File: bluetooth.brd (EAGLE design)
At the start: 28.3 x 23.1 mm, 28 parts, among them U1 NRF8001, X1 16MHz, X2 32.768kHz

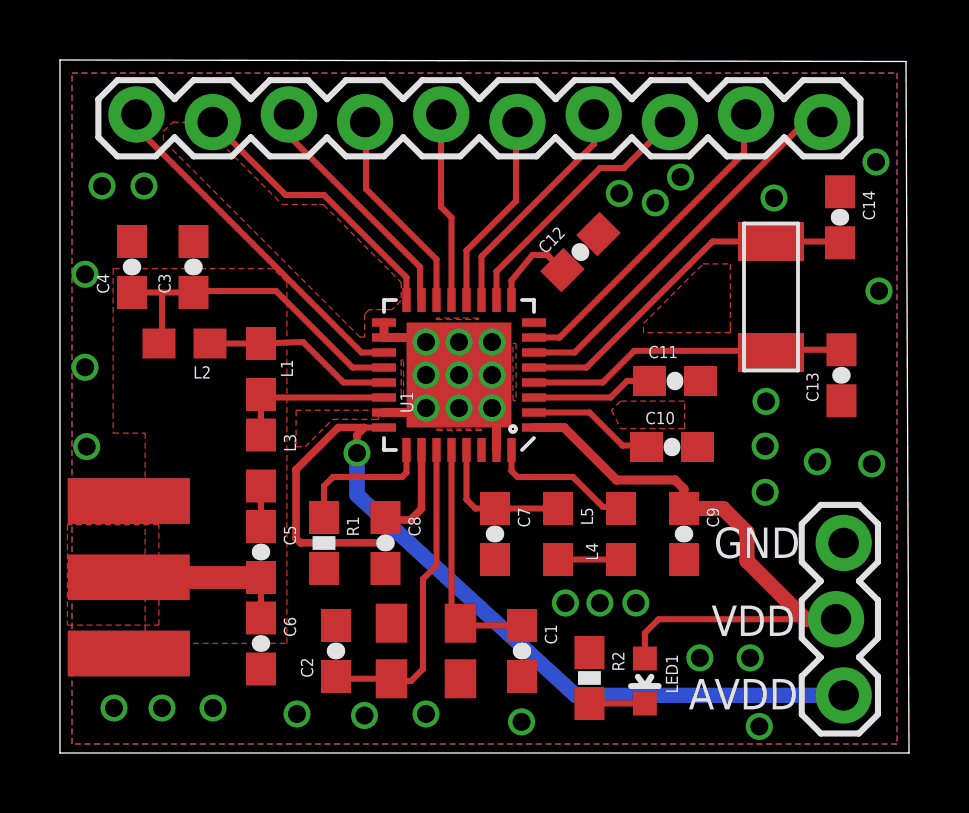
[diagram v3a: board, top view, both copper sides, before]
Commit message: Connected pin 9 (power) to VDD. Oops
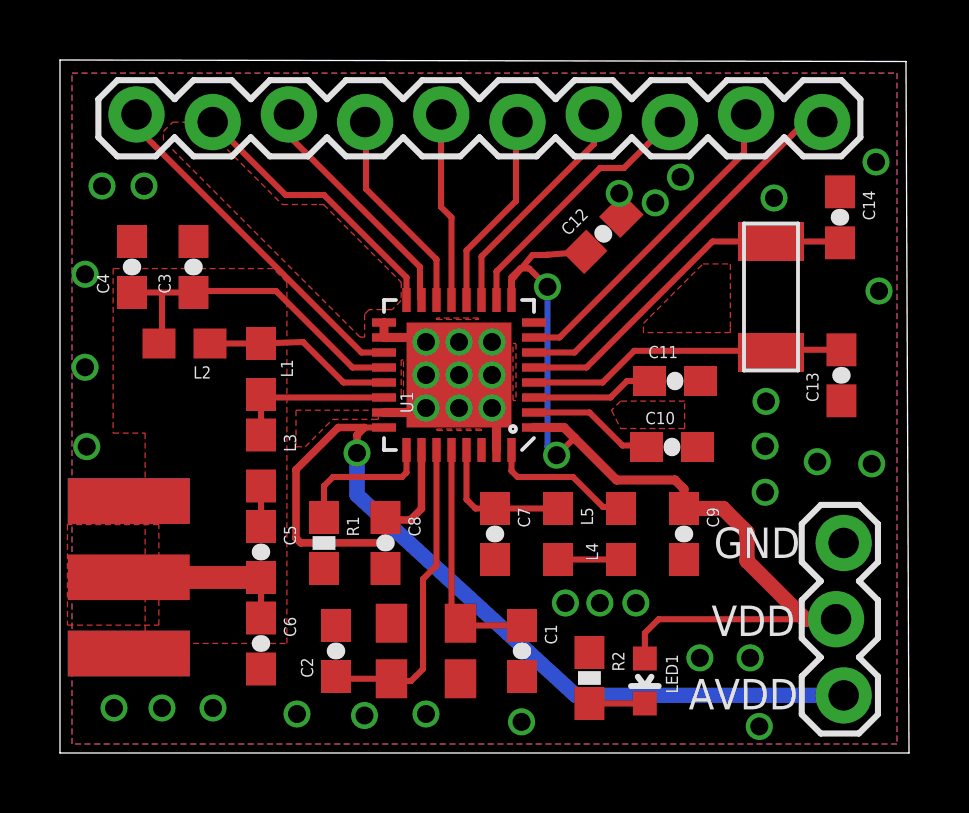
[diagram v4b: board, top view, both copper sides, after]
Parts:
- moved C12 0.98 mm to (17.7, 17.0)
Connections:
- removed net N$8: C12.1, U1.9
- net VDD: now also C12.1, U1.9
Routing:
- net VDD: track 20.5 -> 32.9 mm, vias 0 -> 2
- net N$8: track 2.99 -> 0.00 mm
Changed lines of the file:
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@@
 <setting verticaltext="up"/>
 </settings>
-<grid distance="6" unitdist="mil" unit="inch" style="lines" multiple="1" display="yes" altdistance="0.05" altunitdist="mm" altunit="mm"/>
+<grid distance="1" unitdist="mil" unit="mil" style="lines" multiple="1" display="yes" altdistance="0.05" altunitdist="mm" altunit="mm"/>
 <layers>
 <layer number="1" name="Top" color="4" fill="1" visible="yes" active="yes"/>
@@
 <element name="C13" library="SparkFun" package="0603-CAP" value="12.5pF" x="25.6476125" y="12.29040625" rot="R90"/>
 <element name="C14" library="SparkFun" package="0603-CAP" value="12.5pF" x="25.6000125" y="17.557209375" rot="R270"/>
-<element name="C12" library="SparkFun" package="0603-CAP" value="100nF" x="16.9476" y="16.3976" rot="R45"/>
+<element name="C12" library="SparkFun" package="0603-CAP" value="100nF" x="17.7096" y="17.0072" rot="R45"/>
 <element name="C3" library="SparkFun" package="0603-CAP" value="2.2nF" x="4.05" y="15.9" rot="R90"/>
 <element name="C4" library="SparkFun" package="0603-CAP" value="0" x="2" y="15.9" rot="R90"/>
@@
 <wire x1="19.250003125" y1="12.1" x2="19.250009375" y2="12.10000625" width="0.2032" layer="1"/>
 </signal>
-<signal name="N$8">
-<contactref element="U1" pad="9"/>
-<contactref element="C12" pad="1"/>
-<wire x1="14.65000625" y1="14.80000625" x2="14.65000625" y2="15.45000625" width="0.2032" layer="1"/>
-<wire x1="14.65000625" y1="15.45000625" x2="15.347609375" y2="16.300009375" width="0.2032" layer="1"/>
-<wire x1="15.347609375" y1="16.300009375" x2="15.6972" y2="16.300009375" width="0.2032" layer="1"/>
-<wire x1="15.6972" y1="16.300009375" x2="15.8496" y2="16.3068" width="0.2032" layer="1"/>
-<wire x1="15.8496" y1="16.3068" x2="15.8363125" y2="16.3068" width="0.2032" layer="1"/>
-<wire x1="15.8363125" y1="16.3068" x2="16.34655625" y2="15.79655625" width="0.2032" layer="1"/>
-</signal>
 <signal name="N$3">
 <contactref element="L3" pad="1"/>
@@
 <wire x1="20.400009375" y1="8.50000625" x2="20.100009375" y2="8.80000625" width="0.3048" layer="1"/>
 <wire x1="20.100009375" y1="8.80000625" x2="18.14999375" y2="8.80000625" width="0.3048" layer="1"/>
-<wire x1="18.14999375" y1="8.80000625" x2="16.4" y2="10.55" width="0.3048" layer="1"/>
+<wire x1="18.14999375" y1="8.80000625" x2="16.7516" y2="10.1984" width="0.3048" layer="1"/>
+<wire x1="16.7516" y1="10.1984" x2="16.4" y2="10.55" width="0.3048" layer="1"/>
 <wire x1="16.4" y1="10.55" x2="15.4000125" y2="10.55" width="0.3048" layer="1"/>
 <wire x1="15.4000125" y1="10.55" x2="15.40000625" y2="10.55000625" width="0.3048" layer="1"/>
@@
 <vertex x="12.15" y="10.45"/>
 </polygon>
+<contactref element="U1" pad="9"/>
+<contactref element="C12" pad="1"/>
+<wire x1="14.65000625" y1="14.80000625" x2="14.65000625" y2="15.45000625" width="0.2032" layer="1"/>
+<wire x1="14.65000625" y1="15.45000625" x2="15.347609375" y2="16.300009375" width="0.2032" layer="1"/>
+<wire x1="15.347609375" y1="16.300009375" x2="15.6972" y2="16.300009375" width="0.2032" layer="1"/>
+<wire x1="15.6972" y1="16.300009375" x2="15.8496" y2="16.3068" width="0.2032" layer="1"/>
+<wire x1="15.8496" y1="16.3068" x2="15.8363125" y2="16.3068" width="0.2032" layer="1"/>
+<wire x1="15.8363125" y1="16.3068" x2="17.10855625" y2="16.40615625" width="0.2032" layer="1"/>
+<wire x1="14.65000625" y1="14.80000625" x2="14.65000625" y2="15.56440625" width="0.2032" layer="1"/>
+<wire x1="14.65000625" y1="15.56440625" x2="14.9352" y2="15.8496" width="0.2032" layer="1"/>
+<wire x1="14.9352" y1="15.8496" x2="15.24" y2="15.8496" width="0.2032" layer="1"/>
+<wire x1="15.24" y1="15.8496" x2="15.8496" y2="15.24" width="0.2032" layer="1"/>
+<via x="15.8496" y="15.24" extent="1-16" drill="0.6" shape="square"/>
+<wire x1="15.8496" y1="15.24" x2="15.8496" y2="9.906" width="0.2032" layer="16"/>
+<wire x1="15.8496" y1="9.906" x2="16.1544" y2="9.6266" width="0.2032" layer="16"/>
+<via x="16.1544" y="9.6266" extent="1-16" drill="0.6"/>
+<wire x1="16.1544" y1="9.6266" x2="16.7516" y2="10.1984" width="0.2032" layer="1"/>
 </signal>
 <signal name="AVDD">
